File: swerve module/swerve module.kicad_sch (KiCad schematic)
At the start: 8 parts

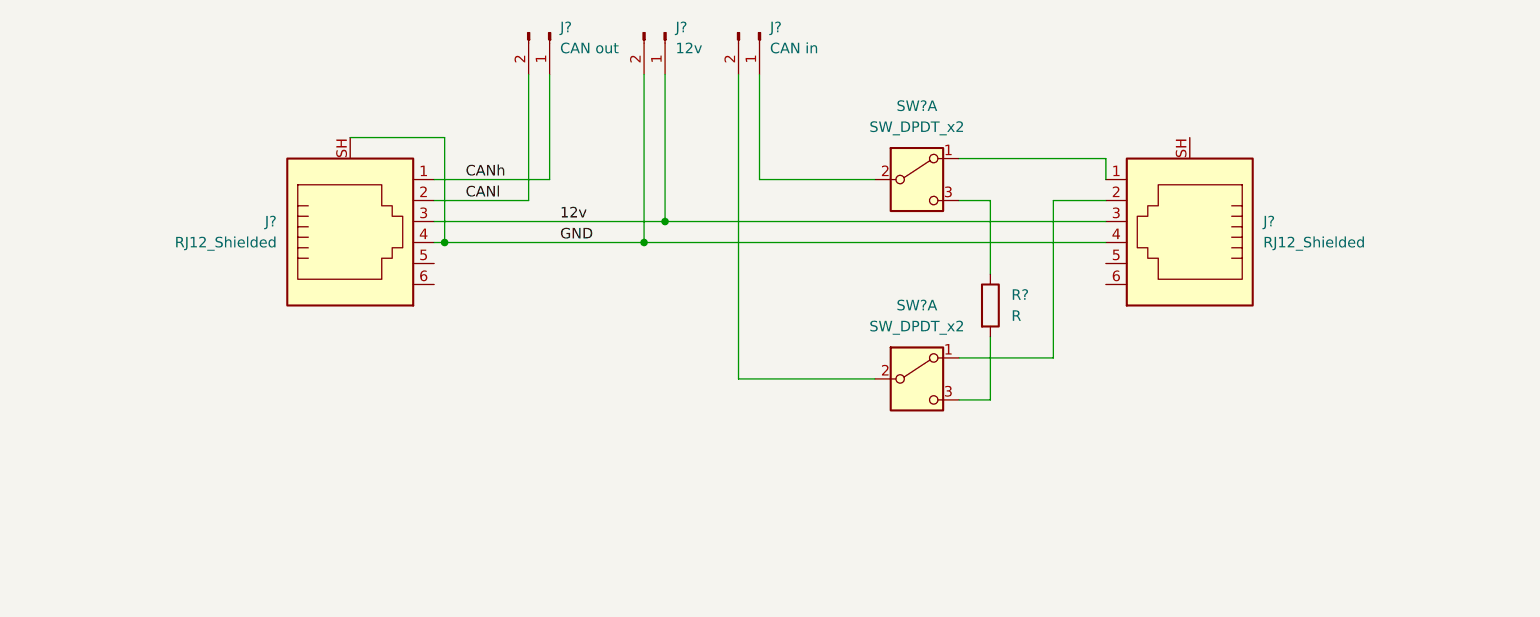
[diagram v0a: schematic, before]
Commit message: swerve can improvements, ground planes, removed excess wagos
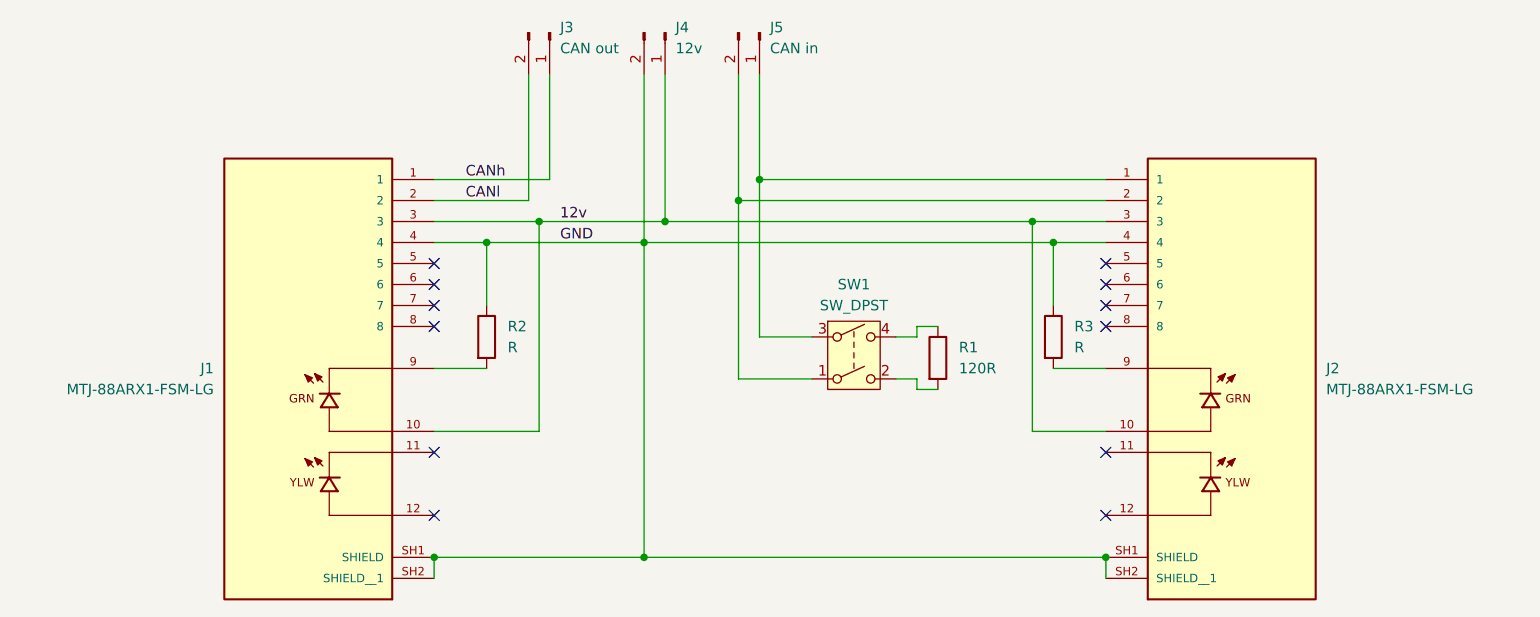
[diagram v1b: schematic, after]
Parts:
- removed J? (x2): RJ12_Shielded, symbol Connector:RJ12_Shielded
- removed SW? (x2): SW_DPDT_x2, symbol Switch:SW_DPDT_x2
- added J1, J2: MTJ-88ARX1-FSM-LG, custom:ADAMTECH_MTJ-88ARX1-FSM-LG, symbol MTJ-88ARX1-FSM-LG:MTJ-88ARX1-FSM-LG
- added R2, R3: R, Resistor_THT:R_Axial_DIN0207_L6.3mm_D2.5mm_P10.16mm_Horizontal, symbol Device:R
- added SW1: SW_DPST, custom:206-211, symbol Switch:SW_DPST
- J3, J4, J5: renamed from J?; footprint (none) -> custom:TerminalBlock_WAGO_2601-1102_1x02_P3.50mm_Horizontal w-model
- R1: renamed from R?; value R -> 120R; footprint (none) -> Resistor_THT:R_Axial_DIN0207_L6.3mm_D2.5mm_P10.16mm_Horizontal
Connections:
- net 12v: now also J1.10, J1.3, J2.10, J2.3
- net CANh: now also J1.1
- net CANl: now also J1.2
- net GND: now also J1.4, J1.SH1 (SHIELD), J1.SH2 (SHIELD__1), J2.4, J2.SH1 (SHIELD), J2.SH2 (SHIELD__1), R2.1, R3.1
- net at R1.1: now also SW1.4
- net at R1.2: now also SW1.2
- net at J5.1 (Pin_1): now also J2.1, SW1.3
- net at J5.2 (Pin_2): now also J2.2, SW1.1
- new net: J2.9, R3.2
- new net: J1.9, R2.2
- no-connect marks 0 -> 12
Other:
- moved on the sheet: R1
